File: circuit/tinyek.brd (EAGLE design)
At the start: 36.5 x 47 mm, 13 parts, among them IC1 ATTiny13A, Q1 2N7000

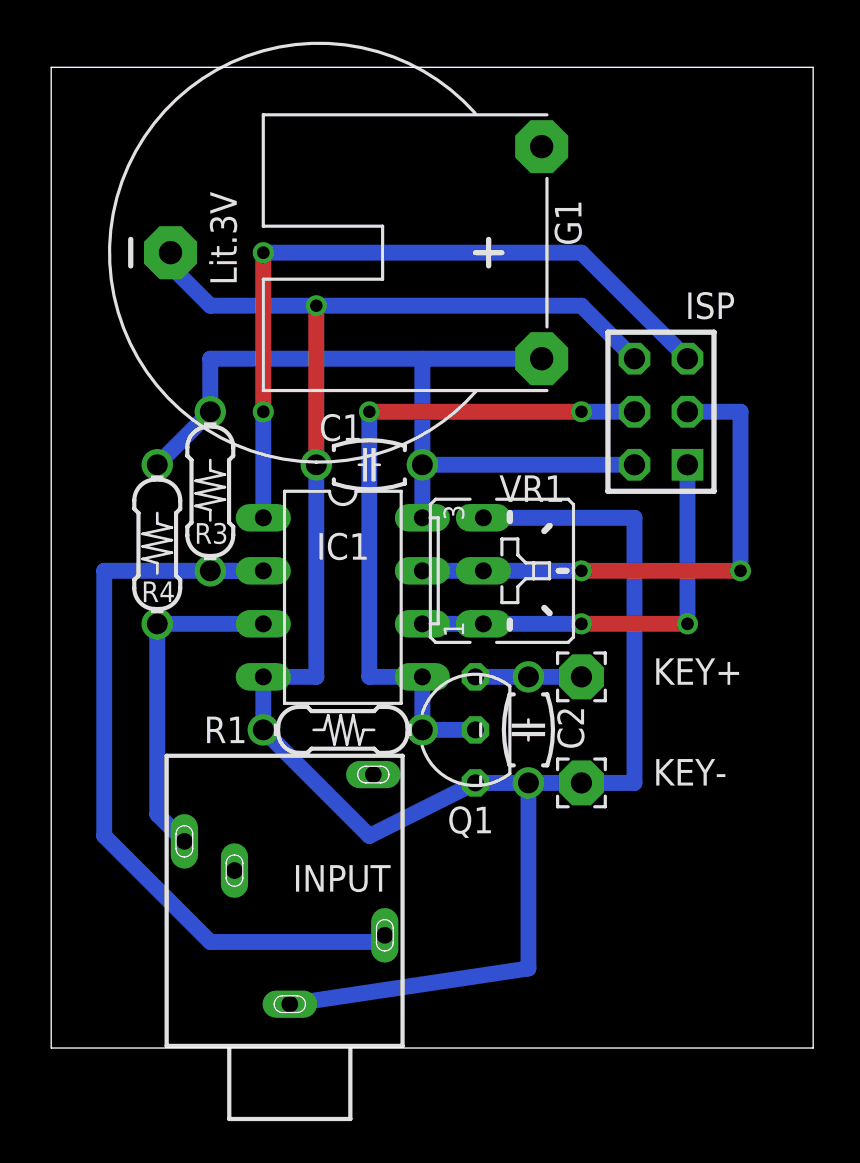
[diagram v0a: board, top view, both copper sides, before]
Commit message: ピンによってドライブ能力が違うので、一応余裕がある配置に設計変更。ほんと意味はないと思う
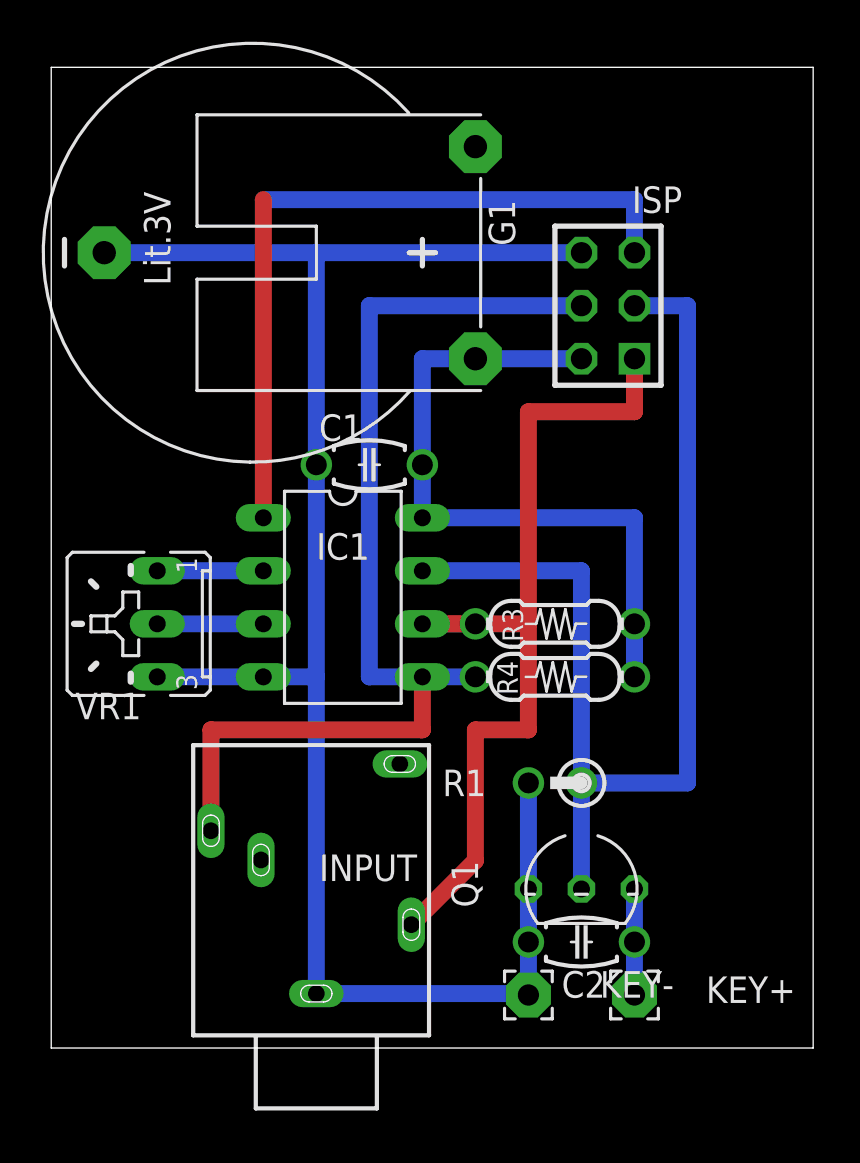
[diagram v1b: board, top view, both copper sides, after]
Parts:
- R1: device r-j:1/4W-7.62H -> r-j:1/4W-2.54V
- moved R4 20.1 mm to (54.6, 20.3), turned to 180 degrees
- moved R3 17.7 mm to (54.6, 22.9), turned to 180 degrees
- moved VR1 17.6 mm to (34.7, 22.9), turned to 90 degrees
- moved KEY+ 15.5 mm to (58.4, 5.08)
- moved R1 11.7 mm to (55.9, 15.2)
- moved C2 10.5 mm to (55.9, 7.62), turned to 180 degrees
- moved KEY- 10.5 mm to (53.3, 5.08)
- moved Q1 9.16 mm to (55.9, 10.2), turned to 0 degrees
- moved ISP 5.68 mm to (57.1, 38.1)
- moved G1 3.17 mm to (40.0, 40.6)
- moved INPUT 1.37 mm to (43.2, 3.05)
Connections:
- removed net N$7: IC1.3, INPUT.3, R4.PAD2
- new net N$10: IC1.5, INPUT.3, ISP.4, R4.PAD2
- net N$4: now also IC1.7, ISP.3; no longer IC1.5, ISP.4
- net N$5: now also IC1.2; no longer IC1.6, ISP.1
- net N$6: now also IC1.3; no longer IC1.7, ISP.3
- net N$8: now also IC1.6, ISP.1; no longer IC1.2
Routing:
- net N$10: track 0.00 -> 50.6 mm
- net GND: track 109.7 -> 86.4 mm, vias 2 -> 0
- net N$6: track 25.4 -> 5.08 mm, vias 2 -> 0
- net N$4: track 33.0 -> 53.3 mm, vias 3 -> 0
- net N$7: track 16.0 -> 0.00 mm
- net N$5: track 20.3 -> 5.08 mm, vias 2 -> 0
- net N$8: track 38.7 -> 43.6 mm
- net VCC: track 39.8 -> 35.6 mm
- net N$1: track 35.1 -> 35.6 mm, vias 2 -> 0

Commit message: update
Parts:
- added ZD1, ZD2: 5V, diode:DO35Z10
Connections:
- net GND: now also ZD1.A, ZD2.A
- net N$10: now also ZD1.C
- net N$8: now also ZD2.C
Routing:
- net GND: track 86.4 -> 94.1 mm
- net N$10: track 50.6 -> 56.2 mm
- net N$1: vias 0 -> 1
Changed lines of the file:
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@@
 <attribute name="VALUE" x="53.975" y="34.29" size="1.27" layer="27" ratio="12" rot="R90"/>
 </element>
+<element name="ZD1" library="diode" package="DO35Z10" value="5V" x="35.56" y="10.16" rot="R270"/>
+<element name="ZD2" library="diode" package="DO35Z10" value="5V" x="50.8" y="10.16" rot="R270"/>
 </elements>
 <signals>
@@
 <wire x1="40.64" y1="20.32" x2="43.18" y2="20.32" width="0.8128" layer="16"/>
 <wire x1="53.34" y1="5.08" x2="53.34" y2="5.148" width="0.8128" layer="16"/>
-<wire x1="53.34" y1="5.148" x2="43.18" y2="5.148" width="0.8128" layer="16"/>
+<wire x1="53.34" y1="5.148" x2="50.8" y2="5.148" width="0.8128" layer="16"/>
+<wire x1="50.8" y1="5.148" x2="43.18" y2="5.148" width="0.8128" layer="16"/>
 <wire x1="53.34" y1="10.16" x2="53.34" y2="7.62" width="0.8128" layer="16"/>
 <wire x1="53.34" y1="7.62" x2="53.34" y2="5.08" width="0.8128" layer="16"/>
 <wire x1="55.88" y1="40.64" x2="43.18" y2="40.64" width="0.8128" layer="16"/>
+<contactref element="ZD2" pad="A"/>
+<contactref element="ZD1" pad="A"/>
+<wire x1="43.18" y1="5.08" x2="35.56" y2="5.08" width="0.762" layer="16"/>
+<wire x1="43.18" y1="5.08" x2="43.18" y2="5.148" width="0.762" layer="16"/>
+<wire x1="50.8" y1="5.08" x2="50.8" y2="5.148" width="0.762" layer="16"/>
 </signal>
 <signal name="VCC">
@@
 <wire x1="53.34" y1="22.86" x2="53.34" y2="17.78" width="0.8128" layer="1"/>
 <wire x1="53.34" y1="17.78" x2="50.8" y2="17.78" width="0.8128" layer="1"/>
-<wire x1="50.8" y1="17.78" x2="50.8" y2="11.518" width="0.8128" layer="1"/>
-<wire x1="50.8" y1="11.518" x2="47.73" y2="8.448" width="0.8128" layer="1"/>
+<wire x1="50.8" y1="17.78" x2="50.8" y2="15.24" width="0.8128" layer="1"/>
+<contactref element="ZD2" pad="C"/>
+<wire x1="47.73" y1="8.448" x2="47.73" y2="12.17" width="0.8128" layer="16"/>
+<wire x1="47.73" y1="12.17" x2="50.8" y2="15.24" width="0.8128" layer="16"/>
 </signal>
 <signal name="N$9">
@@
 <wire x1="58.42" y1="43.18" x2="40.64" y2="43.18" width="0.8128" layer="16"/>
 <wire x1="40.64" y1="27.94" x2="40.64" y2="43.18" width="0.8128" layer="1"/>
-<wire x1="40.64" y1="43.18" x2="40.64" y2="43.18" width="0" layer="19" extent="1-16"/>
+<via x="40.64" y="43.18" extent="1-16" drill="0.6096"/>
 </signal>
 <signal name="N$3">
@@
 <contactref element="R4" pad="PAD2"/>
 <wire x1="38.1" y1="12.948" x2="38.13" y2="12.948" width="0.8128" layer="1"/>
-<wire x1="48.26" y1="17.78" x2="38.13" y2="17.78" width="0.8128" layer="1"/>
-<wire x1="38.13" y1="17.78" x2="38.13" y2="12.948" width="0.8128" layer="1"/>
 <contactref element="IC1" pad="5"/>
 <contactref element="ISP" pad="4"/>
@@
 <wire x1="45.72" y1="38.1" x2="55.88" y2="38.1" width="0.8128" layer="16"/>
 <wire x1="48.26" y1="17.78" x2="48.26" y2="20.32" width="0.8128" layer="1"/>
+<contactref element="ZD1" pad="C"/>
+<wire x1="35.56" y1="12.7" x2="35.56" y2="15.24" width="0.762" layer="16"/>
+<wire x1="38.1" y1="12.7" x2="35.56" y2="12.7" width="0.762" layer="16"/>
+<wire x1="38.1" y1="12.7" x2="38.13" y2="12.948" width="0.762" layer="16"/>
+<wire x1="48.26" y1="17.78" x2="35.56" y2="17.78" width="0.8128" layer="1"/>
+<wire x1="35.56" y1="17.78" x2="35.56" y2="15.24" width="0.8128" layer="1"/>
 </signal>
 </signals>

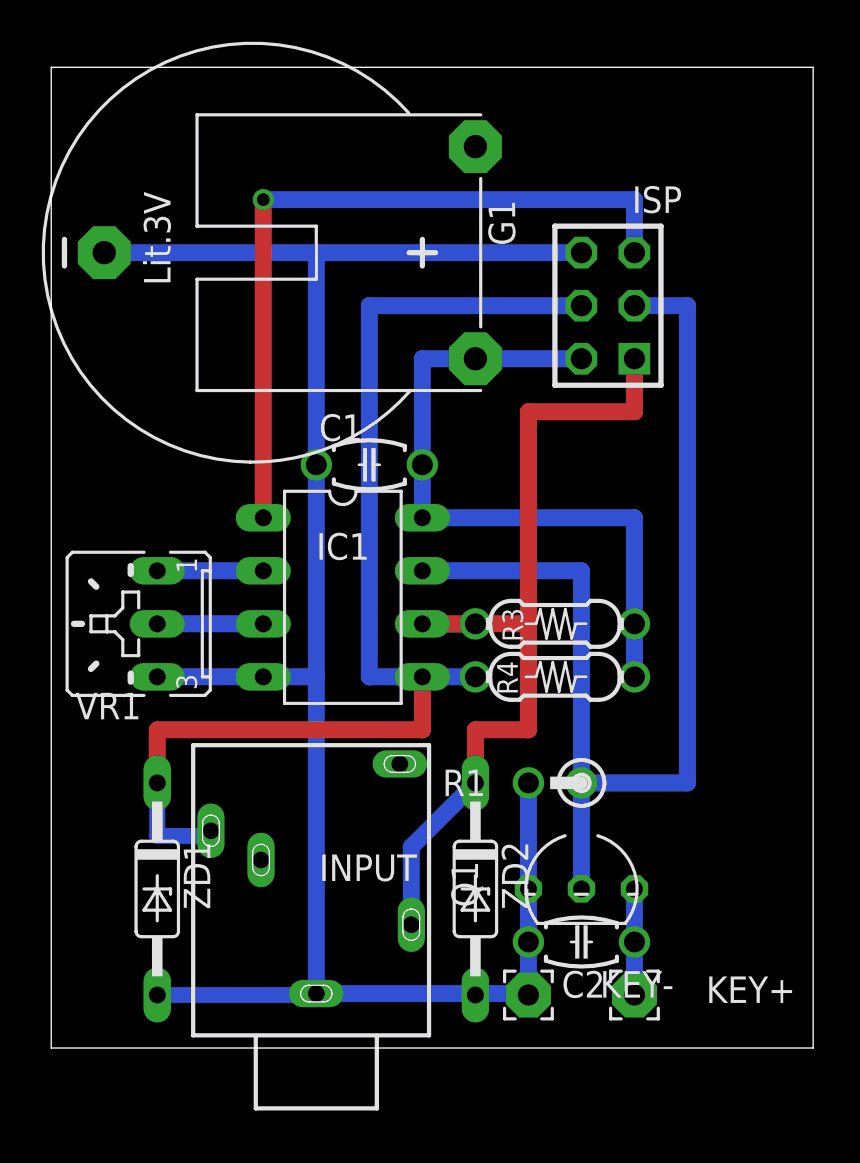
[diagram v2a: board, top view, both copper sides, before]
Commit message: 電流制限抵抗を追加
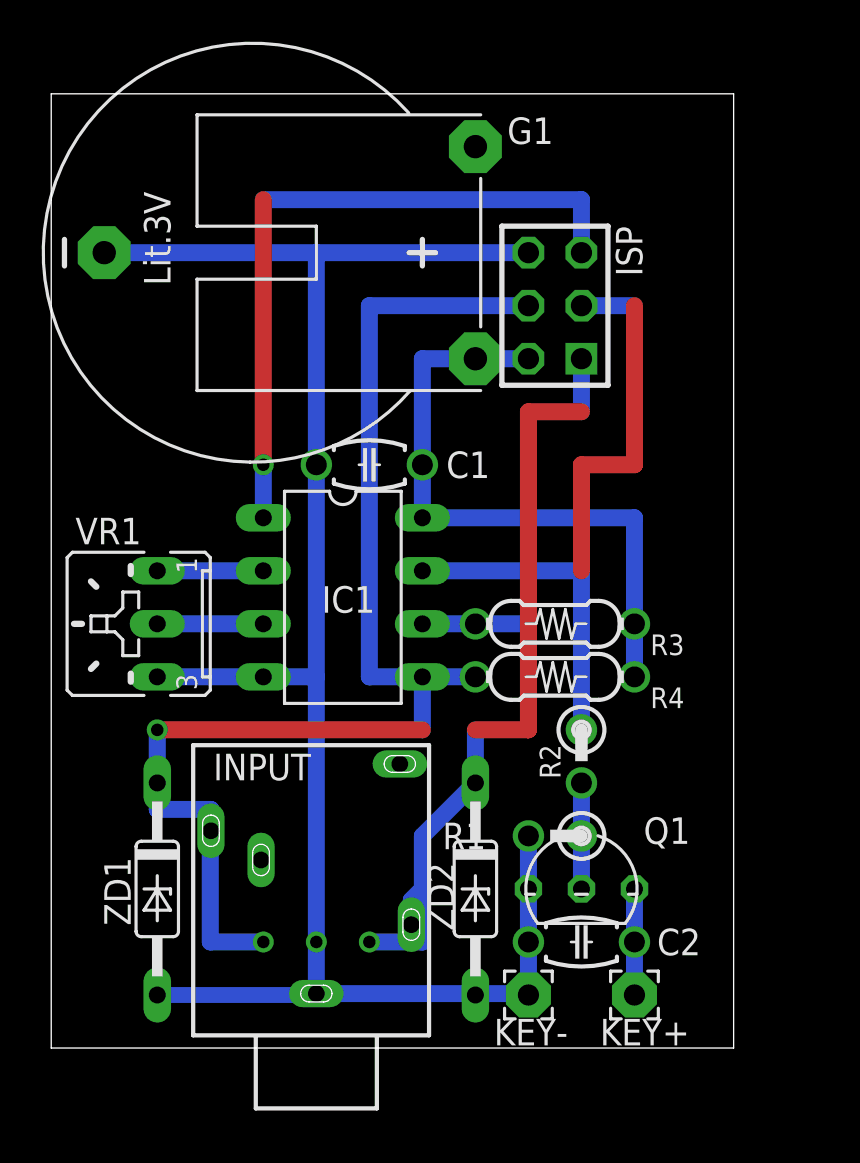
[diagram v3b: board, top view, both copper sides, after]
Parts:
- added R2: 150, r-j:1/4W-2.54V
- moved R1 2.54 mm to (55.9, 12.7)
- moved ISP 2.54 mm to (54.6, 38.1)
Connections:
- new net N$8: Q1.2, R1.PAD1, R2.PAD2
- net N$4: now also R2.PAD1; no longer Q1.2, R1.PAD1
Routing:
- net N$4: track 53.3 -> 33.0 mm
- net N$7: track 0.00 -> 7.62 mm, vias 0 -> 1
- net GND: track 94.1 -> 89.0 mm, vias 0 -> 1
- net N$8: track 0.00 -> 5.08 mm
- net N$10: track 56.2 -> 53.1 mm, vias 0 -> 1
- net N$1: track 35.6 -> 33.0 mm
- net VCC: track 35.6 -> 33.0 mm
- net N$11: vias 0 -> 1
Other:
- board size 36.5 x 47 mm -> 32.7 x 45.7 mm
